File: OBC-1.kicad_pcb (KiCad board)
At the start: 6 copper layers, 42.8 x 42.8 mm, 112 parts, among them J1 ERM8-020-X, J2 ERF6-020-X, J3 Conn_01x02_Female, Q1 MGSF1N02L, Q2 MGSF1N02L, U1 TPS62850x-Q1, U10 FM33256B, U11 TMS5701227CZWTQQ1, U2 TPS62850x-Q1, U3 LTC4353, U4 SN65HVD230M-EP, U5 SN65HVD230M-EP, U6 SN65HVD230M-EP, X1 ASTMTXK-32.768KHZ

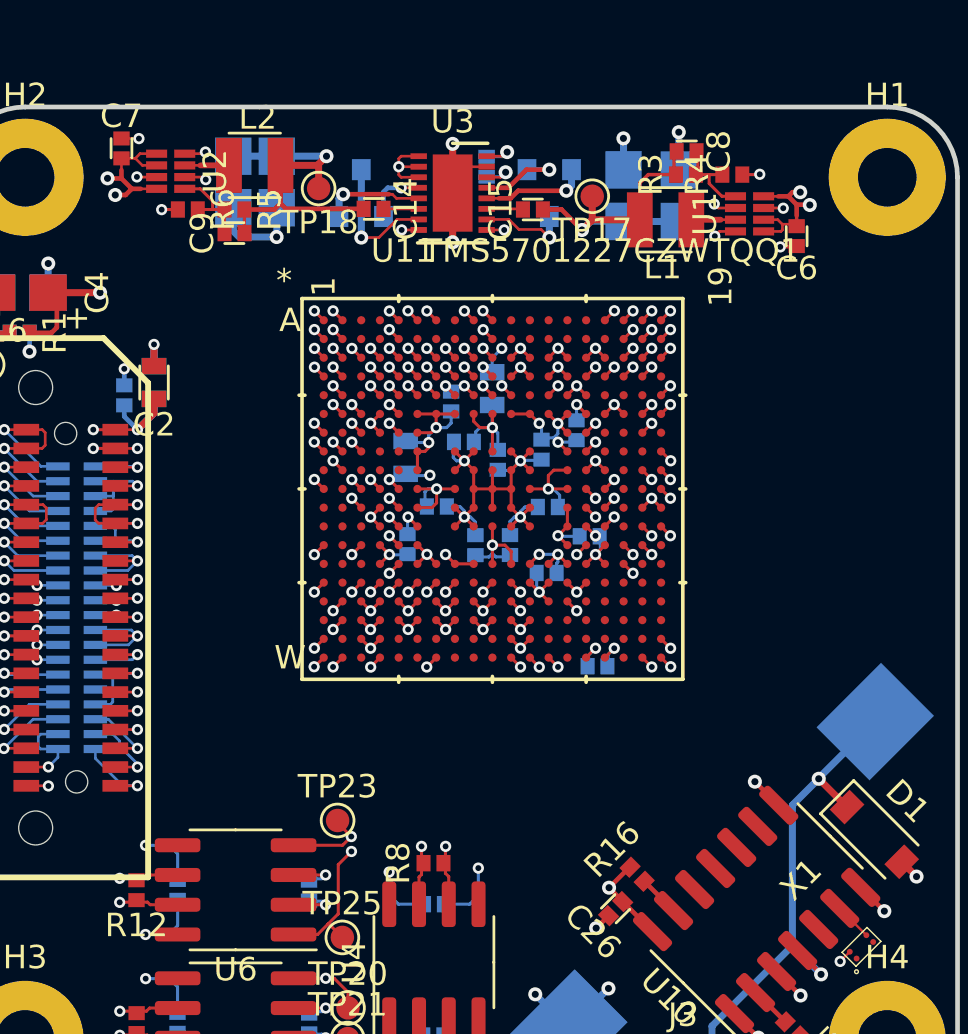
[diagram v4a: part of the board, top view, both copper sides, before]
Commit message: initial SDRAM positioning, need to floorplan remainder of memory ICs
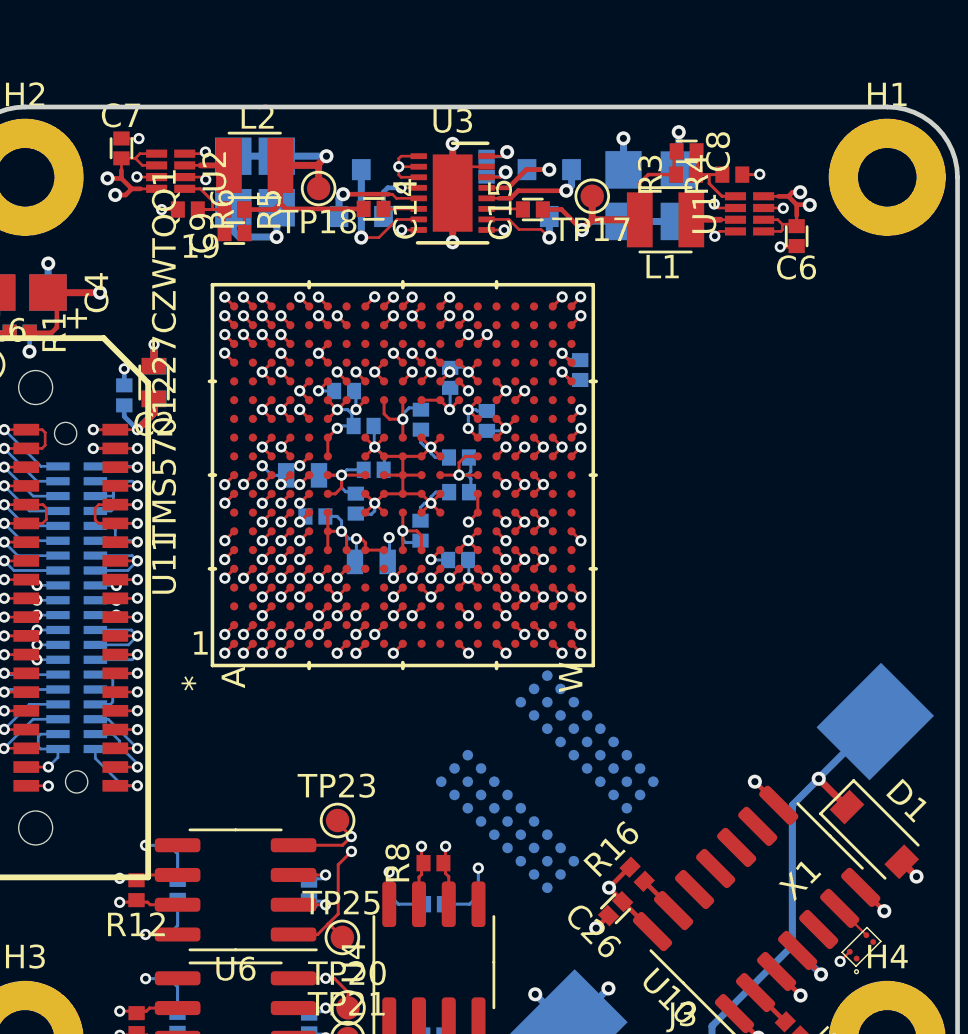
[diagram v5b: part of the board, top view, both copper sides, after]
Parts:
- added U9: IS42S16160J-7BLI, TFT_BGA:TF-BGA_54L_9x9_3colGap_8x8mm, B.Cu at (114.2, 100.3)
- moved C42 12.6 mm to (115.6, 82.8), turned to 180 degrees
- moved C35 10.0 mm to (105.5, 83.6), turned to 270 degrees
- moved C31 8.98 mm to (110.0, 83.1), turned to 180 degrees
- moved C29 8.90 mm to (103.7, 87.2), turned to 90 degrees
- moved C30 7.68 mm to (106.3, 85.1), turned to 90 degrees
- moved C34 7.55 mm to (104.3, 89.0), turned to 270 degrees
- moved C39 7.01 mm to (111.6, 84.9), turned to 0 degrees
- moved C40 6.61 mm to (108.8, 84.8), turned to 0 degrees
- moved C32 5.34 mm to (106.8, 87.0), turned to 90 degrees
- moved C37 5.32 mm to (106.0, 88.4), turned to 0 degrees
- moved C28 4.69 mm to (106.7, 90.9), turned to 270 degrees
- moved C36 4.34 mm to (110.4, 86.5), turned to 270 degrees
- moved U11 3.87 mm to (108.0, 87.2), turned to 90 degrees
- moved C33 2.38 mm to (110.4, 87.9), turned to 270 degrees
- moved C38 2.24 mm to (110.4, 90.8), turned to 90 degrees
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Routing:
- removed copper zone on In3.Cu, net OBC_1V25

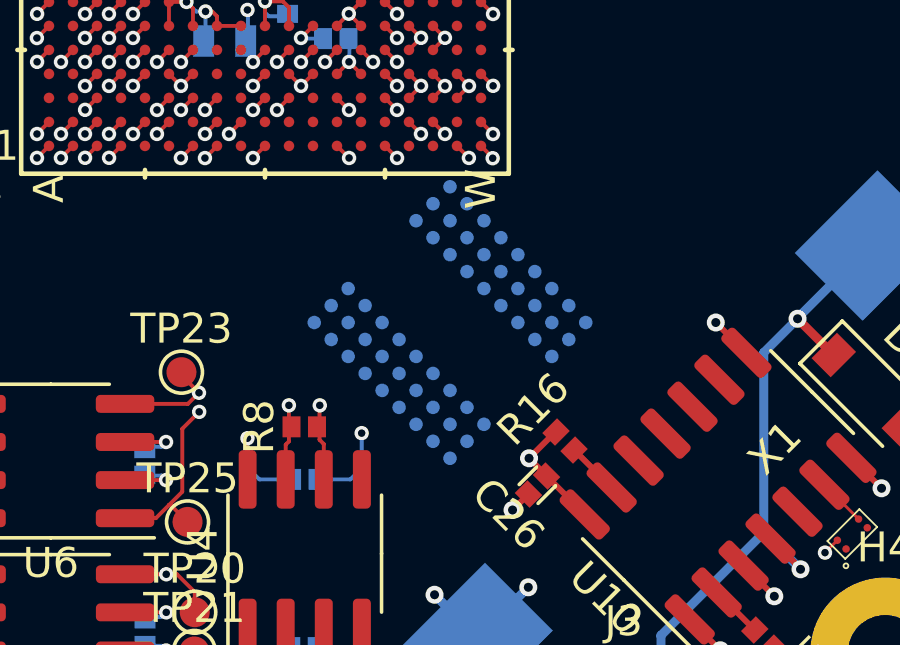
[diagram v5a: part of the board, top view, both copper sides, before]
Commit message: fixed bus netlisting issue - labelling was incorrectly formatted
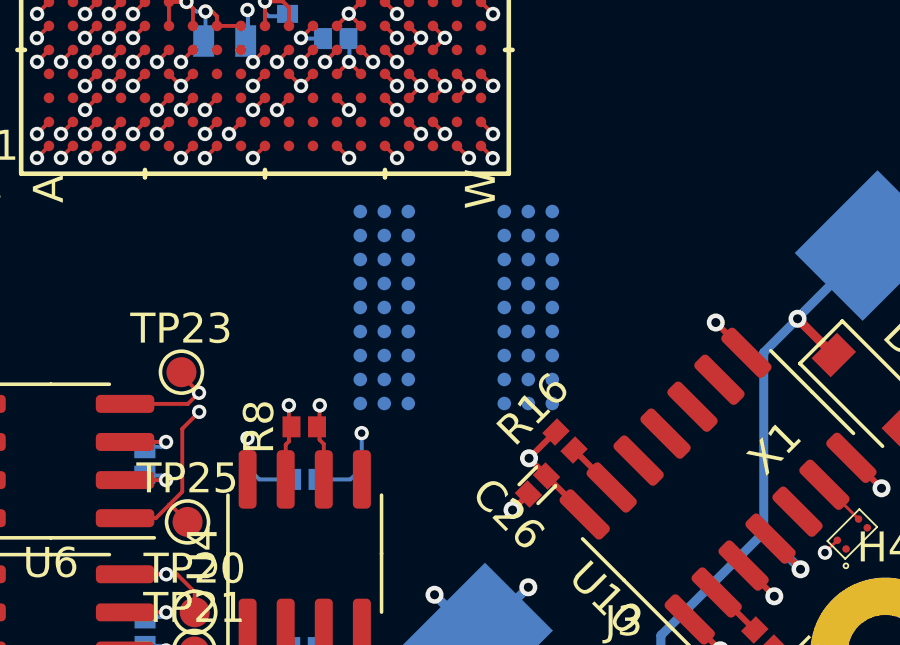
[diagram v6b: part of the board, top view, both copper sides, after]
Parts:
- moved U9 0.54 mm to (114.4, 99.8), turned to 0 degrees
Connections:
- U11 pad C10: /TMS570_uC/A12 -> /SDRAM_1/A12
- U11 pad C4: /TMS570_uC/A6 -> /SDRAM_1/A6
- U11 pad C5: /TMS570_uC/A7 -> /SDRAM_1/A7
- U11 pad C6: /TMS570_uC/A8 -> /SDRAM_1/A8
- U11 pad C7: /TMS570_uC/A9 -> /SDRAM_1/A9
- U11 pad C8: /TMS570_uC/A10 -> /SDRAM_1/A10
- U11 pad C9: /TMS570_uC/A11 -> /SDRAM_1/A11
- U11 pad D16: /TMS570_uC/BA1 -> /SDRAM_1/BA1
- U11 pad D4: /TMS570_uC/A0 -> /SDRAM_1/A0
- U11 pad D5: /TMS570_uC/A1 -> /SDRAM_1/A1
- U11 pad E13: /TMS570_uC/BA0 -> /SDRAM_1/BA0
- U11 pad E5: /TMS570_uC/DQ4 -> /SDRAM_1/DQ4
- U11 pad E6: /TMS570_uC/A2 -> /SDRAM_1/A2
- U11 pad E7: /TMS570_uC/A3 -> /SDRAM_1/A3
- U11 pad E8: /TMS570_uC/A4 -> /SDRAM_1/A4
- U11 pad E9: /TMS570_uC/A5 -> /SDRAM_1/A5
- U11 pad F5: /TMS570_uC/DQ5 -> /SDRAM_1/DQ5
- U11 pad G5: /TMS570_uC/DQ6 -> /SDRAM_1/DQ6
- U11 pad K15: /TMS570_uC/DQ0 -> /SDRAM_1/DQ0
- U11 pad K5: /TMS570_uC/DQ7 -> /SDRAM_1/DQ7
- U11 pad L15: /TMS570_uC/DQ1 -> /SDRAM_1/DQ1
- U11 pad L5: /TMS570_uC/DQ8 -> /SDRAM_1/DQ8
- U11 pad M15: /TMS570_uC/DQ2 -> /SDRAM_1/DQ2
- U11 pad M5: /TMS570_uC/DQ9 -> /SDRAM_1/DQ9
- U11 pad N15: /TMS570_uC/DQ3 -> /SDRAM_1/DQ3
- U11 pad N5: /TMS570_uC/DQ10 -> /SDRAM_1/DQ10
- U11 pad P5: /TMS570_uC/DQ11 -> /SDRAM_1/DQ11
- U11 pad R5: /TMS570_uC/DQ12 -> /SDRAM_1/DQ12
- U11 pad R6: /TMS570_uC/DQ13 -> /SDRAM_1/DQ13
- U11 pad R7: /TMS570_uC/DQ14 -> /SDRAM_1/DQ14
- U11 pad R8: /TMS570_uC/DQ15 -> /SDRAM_1/DQ15
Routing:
- net /TMS570_uC/A5: track 0.57 -> 0.00 mm, vias 1 -> 0
- net /SDRAM_1/A5: track 0.00 -> 0.57 mm, vias 0 -> 1
- net /TMS570_uC/DQ7: track 0.57 -> 0.00 mm, vias 1 -> 0
- net /SDRAM_1/DQ7: track 0.00 -> 0.57 mm, vias 0 -> 1
- net /TMS570_uC/A4: track 0.57 -> 0.00 mm, vias 1 -> 0
- net /SDRAM_1/A4: track 0.00 -> 0.57 mm, vias 0 -> 1
- net /TMS570_uC/A1: track 0.57 -> 0.00 mm, vias 1 -> 0
- net /SDRAM_1/A1: track 0.00 -> 0.57 mm, vias 0 -> 1
- net /TMS570_uC/DQ12: track 0.57 -> 0.00 mm, vias 1 -> 0
- net /SDRAM_1/DQ12: track 0.00 -> 0.57 mm, vias 0 -> 1
- net /TMS570_uC/DQ2: track 0.57 -> 0.00 mm, vias 1 -> 0
- net /TMS570_uC/BA1: track 0.57 -> 0.00 mm, vias 1 -> 0
- net /TMS570_uC/A3: track 0.57 -> 0.00 mm, vias 1 -> 0
- net /SDRAM_1/DQ2: track 0.00 -> 0.57 mm, vias 0 -> 1
- net /SDRAM_1/BA1: track 0.00 -> 0.57 mm, vias 0 -> 1
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
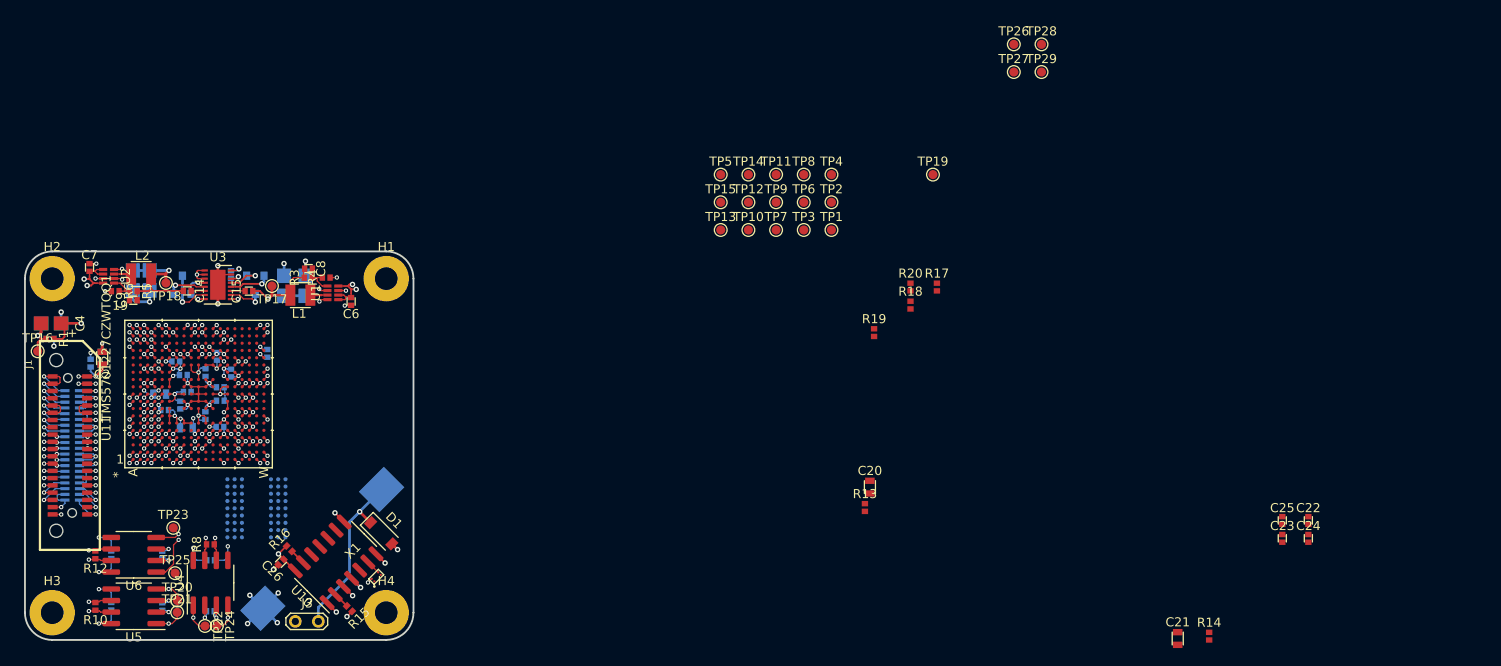
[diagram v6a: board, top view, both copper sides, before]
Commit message: removed SDRAM to simplify initial design
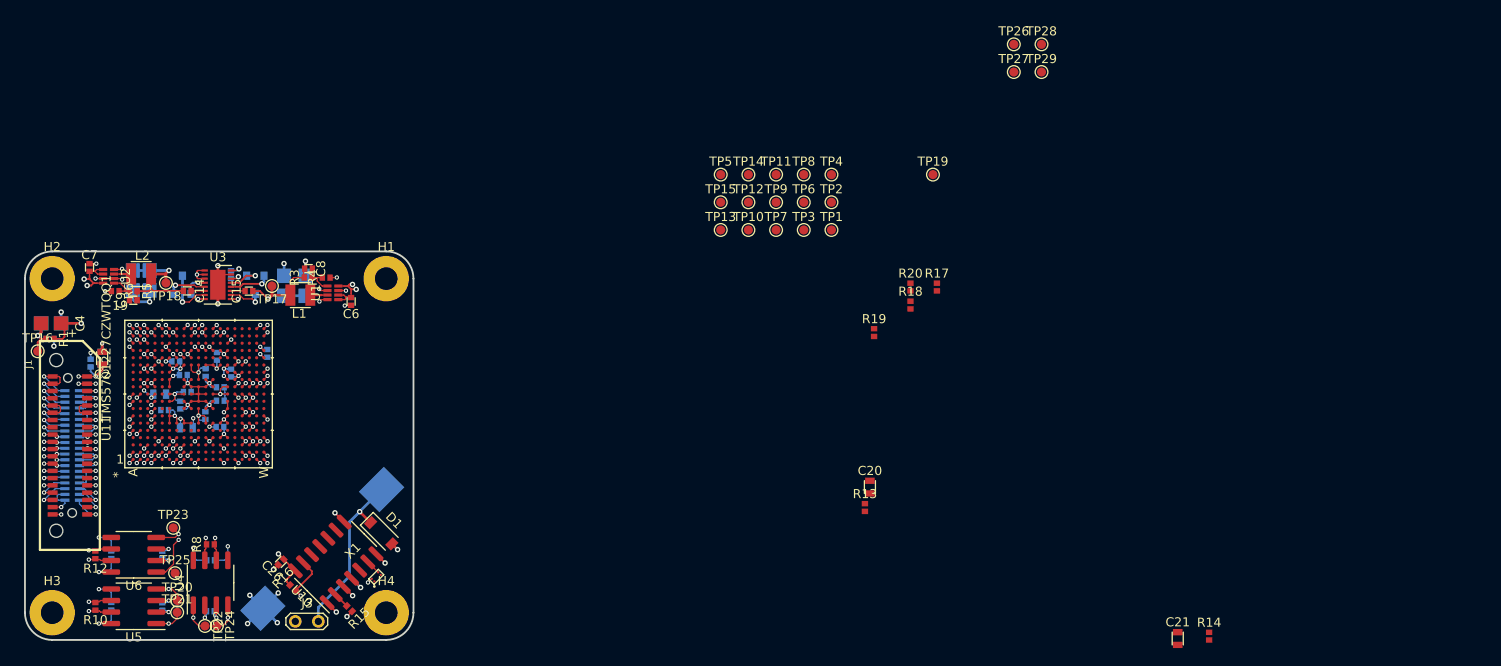
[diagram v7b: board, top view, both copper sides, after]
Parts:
- removed C22, C23, C24, C25: 100n-10V-0402-5%-CER, TFT_C_passive_SMD:0402_CAP
- removed U9: IS42S16160J-7BLI, TFT_BGA:TF-BGA_54L_9x9_3colGap_8x8mm
- moved R16 4.32 mm to (118.4, 108.5)
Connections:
- U11 pad C10: /SDRAM_1/A12 -> Net-(U11-PadC10)
- U11 pad C4: /SDRAM_1/A6 -> Net-(U11-PadC4)
- U11 pad C5: /SDRAM_1/A7 -> Net-(U11-PadC5)
- U11 pad C6: /SDRAM_1/A8 -> Net-(U11-PadC6)
- U11 pad C7: /SDRAM_1/A9 -> Net-(U11-PadC7)
- U11 pad C8: /SDRAM_1/A10 -> Net-(U11-PadC8)
- U11 pad C9: /SDRAM_1/A11 -> Net-(U11-PadC9)
- U11 pad D16: /SDRAM_1/BA1 -> Net-(U11-PadD16)
- U11 pad D17: /SDRAM_1/SDRAM_1_nWE -> Net-(U11-PadD17)
- U11 pad D4: /SDRAM_1/A0 -> Net-(U11-PadD4)
- U11 pad D5: /SDRAM_1/A1 -> Net-(U11-PadD5)
- U11 pad E10: /SDRAM_1/SDRAM_1_DQML -> Net-(U11-PadE10)
- U11 pad E11: /SDRAM_1/SDRAM_1_DQMH -> Net-(U11-PadE11)
- U11 pad E13: /SDRAM_1/BA0 -> Net-(U11-PadE13)
- U11 pad E5: /SDRAM_1/DQ4 -> Net-(U11-PadE5)
- U11 pad E6: /SDRAM_1/A2 -> Net-(U11-PadE6)
- U11 pad E7: /SDRAM_1/A3 -> Net-(U11-PadE7)
- U11 pad E8: /SDRAM_1/A4 -> Net-(U11-PadE8)
- U11 pad E9: /SDRAM_1/A5 -> Net-(U11-PadE9)
- U11 pad F5: /SDRAM_1/DQ5 -> Net-(U11-PadF5)
- U11 pad G5: /SDRAM_1/DQ6 -> Net-(U11-PadG5)
- U11 pad K15: /SDRAM_1/DQ0 -> Net-(U11-PadK15)
- U11 pad K3: /SDRAM_1/SDRAM_1_CLK -> Net-(U11-PadK3)
- U11 pad K5: /SDRAM_1/DQ7 -> Net-(U11-PadK5)
- U11 pad L15: /SDRAM_1/DQ1 -> Net-(U11-PadL15)
- U11 pad L3: /SDRAM_1/SDRAM_1_CKE -> Net-(U11-PadL3)
- U11 pad L5: /SDRAM_1/DQ8 -> Net-(U11-PadL5)
- U11 pad M15: /SDRAM_1/DQ2 -> Net-(U11-PadM15)
- U11 pad M5: /SDRAM_1/DQ9 -> Net-(U11-PadM5)
- U11 pad N15: /SDRAM_1/DQ3 -> Net-(U11-PadN15)
- U11 pad N17: /SDRAM_1/SDRAM_1_nCS -> Net-(U11-PadN17)
- U11 pad N5: /SDRAM_1/DQ10 -> Net-(U11-PadN5)
- U11 pad P5: /SDRAM_1/DQ11 -> Net-(U11-PadP5)
- U11 pad R3: /SDRAM_1/SDRAM_1_nRAS -> Net-(U11-PadR3)
- U11 pad R4: /SDRAM_1/SDRAM_1_nCAS -> Net-(U11-PadR4)
- U11 pad R5: /SDRAM_1/DQ12 -> Net-(U11-PadR5)
- U11 pad R6: /SDRAM_1/DQ13 -> Net-(U11-PadR6)
- U11 pad R7: /SDRAM_1/DQ14 -> Net-(U11-PadR7)
- U11 pad R8: /SDRAM_1/DQ15 -> Net-(U11-PadR8)
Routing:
- net /Supervisor_RTC_FRAM/SPVSR_ACS: track 2.34 -> 5.56 mm, vias 1 -> 2
- net OBC_3V3: track 80.3 -> 82.0 mm
- net /SDRAM_1/A5: track 0.57 -> 0.00 mm, vias 1 -> 0
- net /SDRAM_1/DQ7: track 0.57 -> 0.00 mm, vias 1 -> 0
- net /SDRAM_1/SDRAM_1_DQML: track 0.57 -> 0.00 mm, vias 1 -> 0
- net /SDRAM_1/A4: track 0.57 -> 0.00 mm, vias 1 -> 0
- net /SDRAM_1/A1: track 0.57 -> 0.00 mm, vias 1 -> 0
- net /SDRAM_1/DQ12: track 0.57 -> 0.00 mm, vias 1 -> 0
- net /SDRAM_1/DQ2: track 0.57 -> 0.00 mm, vias 1 -> 0
- net /SDRAM_1/BA1: track 0.57 -> 0.00 mm, vias 1 -> 0
- net /SDRAM_1/A3: track 0.57 -> 0.00 mm, vias 1 -> 0
- net /SDRAM_1/DQ4: track 0.57 -> 0.00 mm, vias 1 -> 0
- net /SDRAM_1/DQ14: track 0.57 -> 0.00 mm, vias 1 -> 0
- net /SDRAM_1/DQ13: track 0.57 -> 0.00 mm, vias 1 -> 0
- net /SDRAM_1/DQ5: track 0.57 -> 0.00 mm, vias 1 -> 0
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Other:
- net class Default: clearance 0.15 -> 0.1
- rule trace_clearance: 0.15 -> 0.1

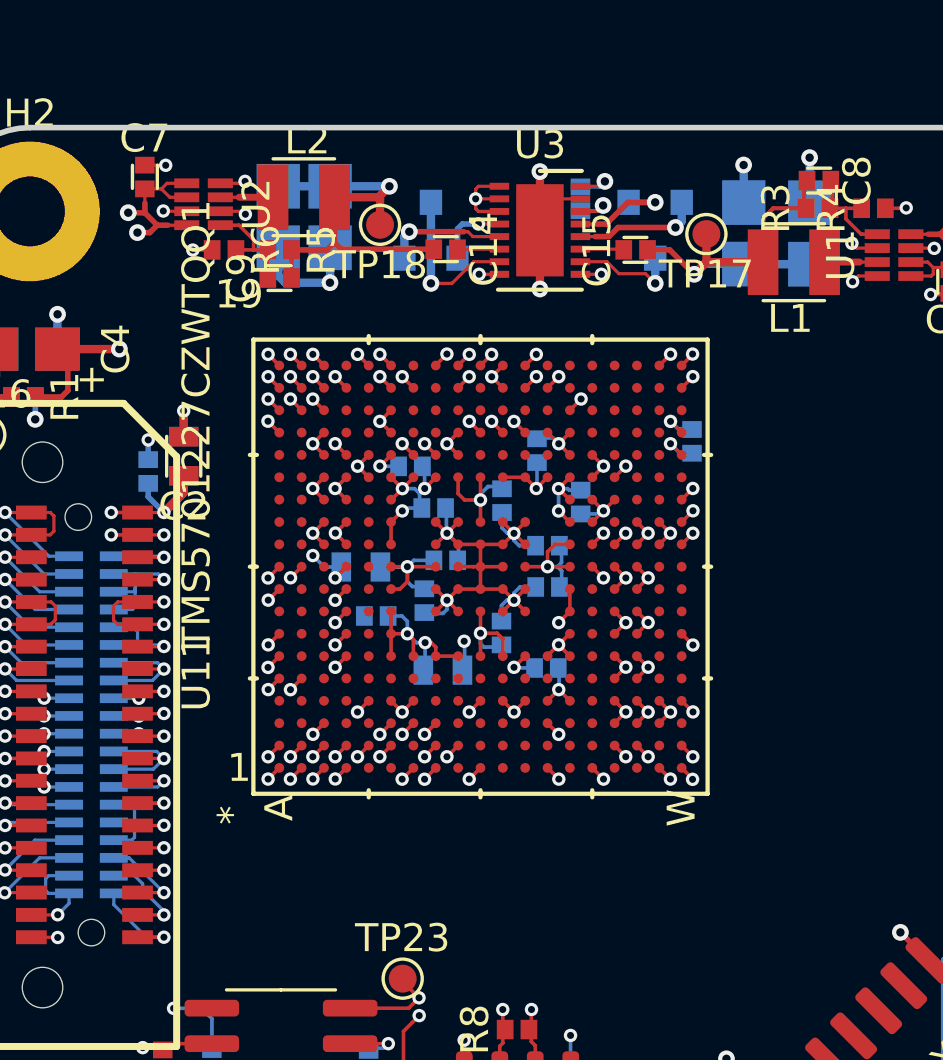
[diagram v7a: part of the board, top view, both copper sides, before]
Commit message: fixed typo in GPS net label
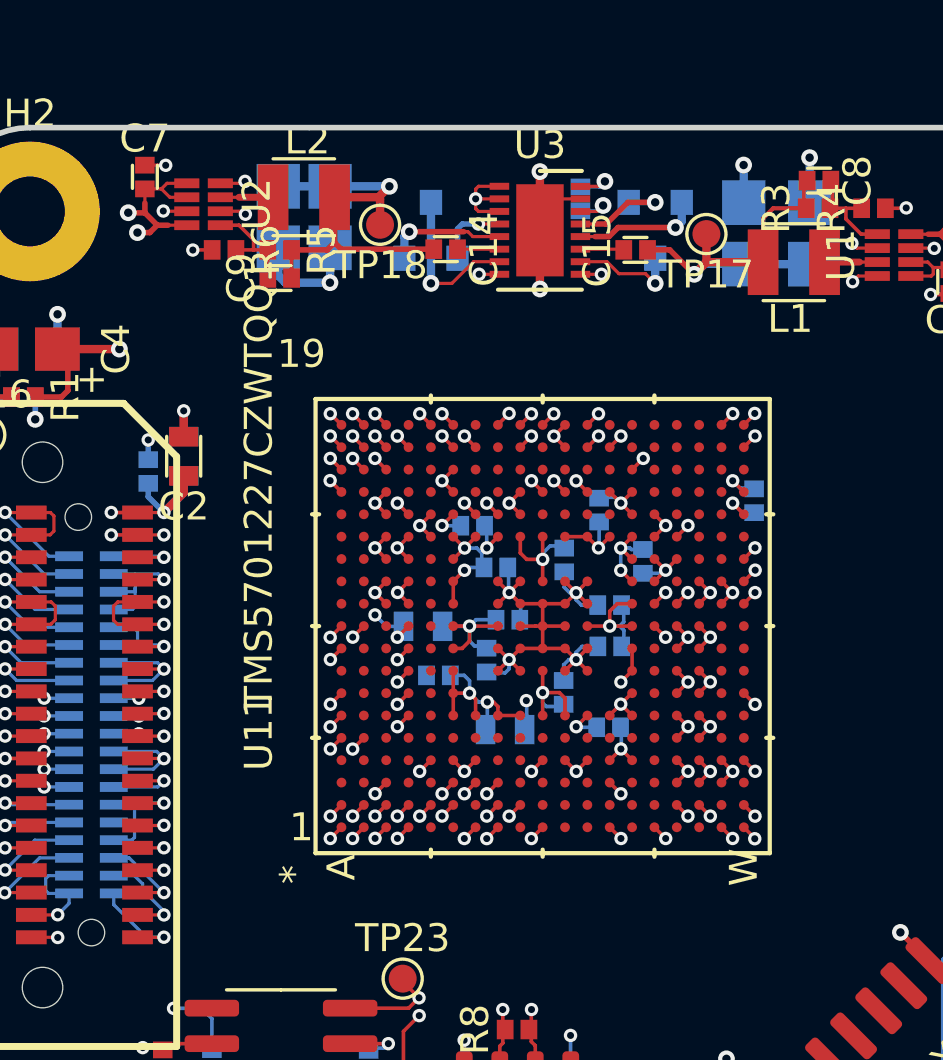
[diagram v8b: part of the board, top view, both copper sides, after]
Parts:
- moved C28 3.08 mm to (108.9, 93.0)
- moved C32 3.08 mm to (109.0, 89.1)
- moved C33 3.08 mm to (112.7, 90.1)
- moved C34 3.08 mm to (106.5, 91.1)
- moved C36 3.08 mm to (112.7, 88.6)
- moved C40 3.08 mm to (111.0, 86.9)
- moved C41 3.08 mm to (111.0, 91.7)
- moved C29 3.08 mm to (106.0, 89.3)
- moved C30 3.08 mm to (108.5, 87.2)
- moved C31 3.08 mm to (112.3, 85.2)
- moved C35 3.08 mm to (107.8, 85.7)
- moved C37 3.08 mm to (108.2, 90.5)
- moved C38 3.08 mm to (112.6, 93.0)
- moved C39 3.08 mm to (113.8, 87.0)
- moved C42 3.08 mm to (117.8, 84.9)
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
